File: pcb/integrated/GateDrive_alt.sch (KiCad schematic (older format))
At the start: 14 parts, among them U11001 UCC5350SB, U11002 R15P21503D

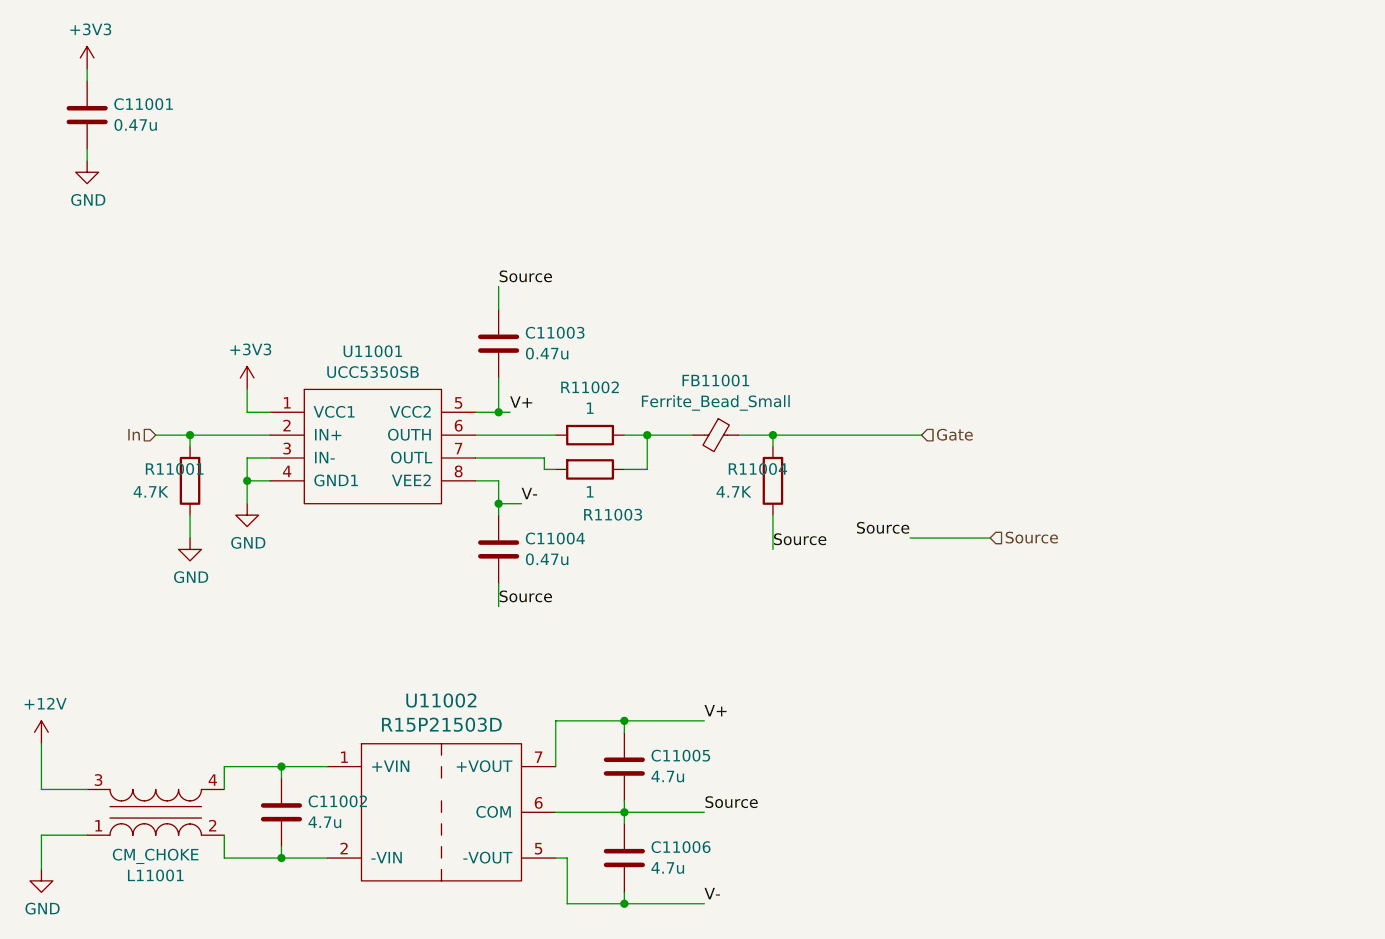
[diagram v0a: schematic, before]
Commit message: revised power input schematic
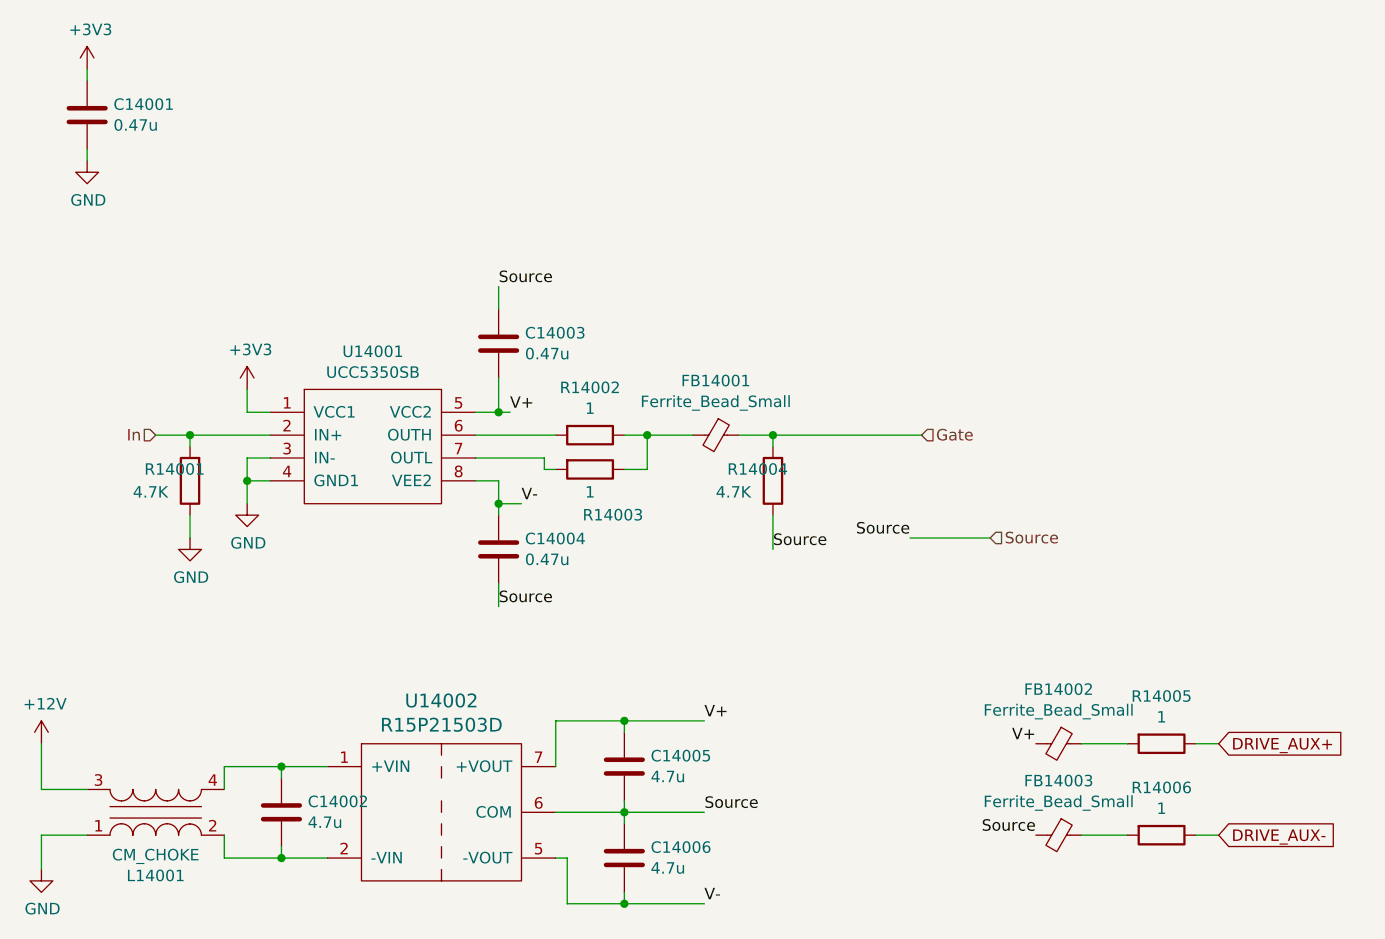
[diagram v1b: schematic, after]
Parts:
- added FB11002, FB11003: Ferrite_Bead_Small, Inductor_SMD:L_0805_2012Metric, symbol Device:Ferrite_Bead_Small
- added R11005, R11006: 1, Resistor_SMD:R_0805_2012Metric, symbol Device:R
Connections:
- net Source: now also FB11003.2
- net V+: now also FB11002.2
- new net: FB11002.1, R11005.2
- new net: FB11003.1, R11006.2
- new net DRIVE_AUX+: R11005.1
- new net DRIVE_AUX-: R11006.1
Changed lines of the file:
@@
 AR Path="/5D68A538/5D640674/5D6308ED" Ref="U13002"  Part="1"
 AR Path="/5D68A538/5D640682/5D6308ED" Ref="U14002"  Part="1"
-F 0 "U11002" H 3450 5237 60  0000 C CNN
+F 0 "U14002" H 3450 5237 60  0000 C CNN
 F 1 "R15P21503D" H 3450 5131 60  0000 C CNN
 F 2 "wbraun_smd:SIP7-5" H 3450 4850 60  0001 C CNN
@@
 AR Path="/5D68A538/5D640674/5D6308F4" Ref="U13001"  Part="1"
 AR Path="/5D68A538/5D640682/5D6308F4" Ref="U14001"  Part="1"
-F 0 "U11001" H 3150 3565 50  0000 C CNN
+F 0 "U14001" H 3150 3565 50  0000 C CNN
 F 1 "UCC5350SB" H 3150 3474 50  0000 C CNN
 F 2 "Package_SO:SOIC-8_3.9x4.9mm_P1.27mm" H 2800 3200 50  0001 C CNN
@@
 AR Path="/5D68A538/5D640674/5D6308FB" Ref="C13002"  Part="1"
 AR Path="/5D68A538/5D640682/5D6308FB" Ref="C14002"  Part="1"
-F 0 "C11002" H 2865 4796 50  0000 L CNN
+F 0 "C14002" H 2865 4796 50  0000 L CNN
 F 1 "4.7u" H 2865 4705 50  0000 L CNN
 F 2 "Capacitor_SMD:C_0805_2012Metric" H 2788 4600 50  0001 C CNN
@@
 AR Path="/5D68A538/5D640674/5D630902" Ref="C13005"  Part="1"
 AR Path="/5D68A538/5D640682/5D630902" Ref="C14005"  Part="1"
-F 0 "C11005" H 4365 4596 50  0000 L CNN
+F 0 "C14005" H 4365 4596 50  0000 L CNN
 F 1 "4.7u" H 4365 4505 50  0000 L CNN
 F 2 "Capacitor_SMD:C_0805_2012Metric" H 4288 4400 50  0001 C CNN
@@
 AR Path="/5D68A538/5D640674/5D630909" Ref="C13006"  Part="1"
 AR Path="/5D68A538/5D640682/5D630909" Ref="C14006"  Part="1"
-F 0 "C11006" H 4365 4996 50  0000 L CNN
+F 0 "C14006" H 4365 4996 50  0000 L CNN
 F 1 "4.7u" H 4365 4905 50  0000 L CNN
 F 2 "Capacitor_SMD:C_0805_2012Metric" H 4288 4800 50  0001 C CNN
@@
 AR Path="/5D68A538/5D640674/5D630910" Ref="C13003"  Part="1"
 AR Path="/5D68A538/5D640682/5D630910" Ref="C14003"  Part="1"
-F 0 "C11003" H 3815 2746 50  0000 L CNN
+F 0 "C14003" H 3815 2746 50  0000 L CNN
 F 1 "0.47u" H 3815 2655 50  0000 L CNN
 F 2 "Capacitor_SMD:C_0603_1608Metric" H 3738 2550 50  0001 C CNN
@@
 AR Path="/5D68A538/5D640674/5D630917" Ref="C13004"  Part="1"
 AR Path="/5D68A538/5D640682/5D630917" Ref="C14004"  Part="1"
-F 0 "C11004" H 3815 3646 50  0000 L CNN
+F 0 "C14004" H 3815 3646 50  0000 L CNN
 F 1 "0.47u" H 3815 3555 50  0000 L CNN
 F 2 "Capacitor_SMD:C_0603_1608Metric" H 3738 3450 50  0001 C CNN
@@
 AR Path="/5D68A538/5D640674/5D63091E" Ref="R13002"  Part="1"
 AR Path="/5D68A538/5D640682/5D63091E" Ref="R14002"  Part="1"
-F 0 "R11002" V 3893 3100 50  0000 C CNN
+F 0 "R14002" V 3893 3100 50  0000 C CNN
 F 1 "1" V 3984 3100 50  0000 C CNN
 F 2 "Resistor_SMD:R_0805_2012Metric" V 4030 3100 50  0001 C CNN
@@
 AR Path="/5D68A538/5D640674/5D630925" Ref="R13003"  Part="1"
 AR Path="/5D68A538/5D640682/5D630925" Ref="R14003"  Part="1"
-F 0 "R11003" V 4300 3350 50  0000 C CNN
+F 0 "R14003" V 4300 3350 50  0000 C CNN
 F 1 "1" V 4200 3250 50  0000 C CNN
 F 2 "Resistor_SMD:R_0805_2012Metric" V 4030 3250 50  0001 C CNN
@@
 AR Path="/5D68A538/5D640674/5D63093F" Ref="#PWR013007"  Part="1"
 AR Path="/5D68A538/5D640682/5D63093F" Ref="#PWR014007"  Part="1"
-F 0 "#PWR011007" H 2600 3150 50  0001 C CNN
+F 0 "#PWR014007" H 2600 3150 50  0001 C CNN
 F 1 "GND" H 2605 3227 50  0000 C CNN
 F 2 "" H 2600 3400 50  0001 C CNN
@@
 AR Path="/5D68A538/5D640674/5D630945" Ref="#PWR013006"  Part="1"
 AR Path="/5D68A538/5D640682/5D630945" Ref="#PWR014006"  Part="1"
-F 0 "#PWR011006" H 2600 2750 50  0001 C CNN
+F 0 "#PWR014006" H 2600 2750 50  0001 C CNN
 F 1 "+3V3" H 2615 3073 50  0000 C CNN
 F 2 "" H 2600 2900 50  0001 C CNN
@@
 AR Path="/5D68A538/5D640674/5D63094B" Ref="R13001"  Part="1"
 AR Path="/5D68A538/5D640682/5D63094B" Ref="R14001"  Part="1"
-F 0 "R11001" H 2550 3250 50  0000 R CNN
+F 0 "R14001" H 2550 3250 50  0000 R CNN
 F 1 "4.7K" H 2600 3350 50  0000 R CNN
 F 2 "Resistor_SMD:R_0603_1608Metric" V 2280 3300 50  0001 C CNN
@@
 AR Path="/5D68A538/5D640674/5D630955" Ref="#PWR013005"  Part="1"
 AR Path="/5D68A538/5D640682/5D630955" Ref="#PWR014005"  Part="1"
-F 0 "#PWR011005" H 2350 3300 50  0001 C CNN
+F 0 "#PWR014005" H 2350 3300 50  0001 C CNN
 F 1 "GND" H 2355 3377 50  0000 C CNN
 F 2 "" H 2350 3550 50  0001 C CNN
@@
 AR Path="/5D68A538/5D640674/5D630960" Ref="C13001"  Part="1"
 AR Path="/5D68A538/5D640682/5D630960" Ref="C14001"  Part="1"
-F 0 "C11001" H 2015 1746 50  0000 L CNN
+F 0 "C14001" H 2015 1746 50  0000 L CNN
 F 1 "0.47u" H 2015 1655 50  0000 L CNN
 F 2 "Capacitor_SMD:C_0603_1608Metric" H 1938 1550 50  0001 C CNN
@@
 AR Path="/5D68A538/5D640674/5D630967" Ref="#PWR013003"  Part="1"
 AR Path="/5D68A538/5D640682/5D630967" Ref="#PWR014003"  Part="1"
-F 0 "#PWR011003" H 1900 1350 50  0001 C CNN
+F 0 "#PWR014003" H 1900 1350 50  0001 C CNN
 F 1 "+3V3" H 1915 1673 50  0000 C CNN
 F 2 "" H 1900 1500 50  0001 C CNN
@@
 AR Path="/5D68A538/5D640674/5D63096D" Ref="#PWR013004"  Part="1"
 AR Path="/5D68A538/5D640682/5D63096D" Ref="#PWR014004"  Part="1"
-F 0 "#PWR011004" H 1900 1650 50  0001 C CNN
+F 0 "#PWR014004" H 1900 1650 50  0001 C CNN
 F 1 "GND" H 1905 1727 50  0000 C CNN
 F 2 "" H 1900 1900 50  0001 C CNN
@@
 AR Path="/5D68A538/5D640674/5D634CBC" Ref="#PWR013002"  Part="1"
 AR Path="/5D68A538/5D640682/5D634CBC" Ref="#PWR014002"  Part="1"
-F 0 "#PWR011002" H 1700 4750 50  0001 C CNN
+F 0 "#PWR014002" H 1700 4750 50  0001 C CNN
 F 1 "GND" H 1705 4827 50  0000 C CNN
 F 2 "" H 1700 5000 50  0001 C CNN
@@
 AR Path="/5D68A538/5D640674/5D634D09" Ref="#PWR013001"  Part="1"
 AR Path="/5D68A538/5D640682/5D634D09" Ref="#PWR014001"  Part="1"
-F 0 "#PWR011001" H 1700 4300 50  0001 C CNN
+F 0 "#PWR014001" H 1700 4300 50  0001 C CNN
 F 1 "+12V" H 1715 4623 50  0000 C CNN
 F 2 "" H 1700 4450 50  0001 C CNN
@@
 AR Path="/5D68A538/5D640674/5D63A672" Ref="FB13001"  Part="1"
 AR Path="/5D68A538/5D640682/5D63A672" Ref="FB14001"  Part="1"
-F 0 "FB11001" V 4413 3100 50  0000 C CNN
+F 0 "FB14001" V 4413 3100 50  0000 C CNN
 F 1 "Ferrite_Bead_Small" V 4504 3100 50  0000 C CNN
 F 2 "Inductor_SMD:L_0805_2012Metric" V 4580 3100 50  0001 C CNN
@@
 AR Path="/5D68A538/5D640674/5D63A754" Ref="R13004"  Part="1"
 AR Path="/5D68A538/5D640682/5D63A754" Ref="R14004"  Part="1"
-F 0 "R11004" H 5100 3250 50  0000 R CNN
+F 0 "R14004" H 5100 3250 50  0000 R CNN
 F 1 "4.7K" H 5150 3350 50  0000 R CNN
 F 2 "Resistor_SMD:R_0603_1608Metric" V 4830 3300 50  0001 C CNN
@@
 AR Path="/5D68A538/5D640674/5D63092C" Ref="L13001"  Part="1"
 AR Path="/5D68A538/5D640682/5D63092C" Ref="L14001"  Part="1"
-F 0 "L11001" H 2200 5028 50  0000 C CNN
+F 0 "L14001" H 2200 5028 50  0000 C CNN
 F 1 "CM_CHOKE" H 2200 4937 50  0000 C CNN
 F 2 "wbraun_smd:SRF2012" V 2200 4750 50  0001 C CNN
@@
 	1    0    0    1
 $EndComp
+$Comp
+L Device:R R?
+U 1 1 5DCA72F3
+P 6600 4450
+AR Path="/5D68A538/5DCA72F3" Ref="R?"  Part="1"
+AR Path="/5D68A538/5D62FC9C/5DCA72F3" Ref="R11005"  Part="1"
+AR Path="/5D68A538/5D640666/5DCA72F3" Ref="R12005"  Part="1"
+AR Path="/5D68A538/5D640674/5DCA72F3" Ref="R13005"  Part="1"
+AR Path="/5D68A538/5D640682/5DCA72F3" Ref="R14005"  Part="1"
+F 0 "R14005" V 6393 4450 50  0000 C CNN
+F 1 "1" V 6484 4450 50  0000 C CNN
+F 2 "Resistor_SMD:R_0805_2012Metric" V 6530 4450 50  0001 C CNN
+F 3 "~" H 6600 4450 50  0001 C CNN
+	1    6600 4450
+	0    1    1    0
+$EndComp
+$Comp
+L Device:R R?
+U 1 1 5DCA9067
+P 6600 4850
+AR Path="/5D68A538/5DCA9067" Ref="R?"  Part="1"
+AR Path="/5D68A538/5D62FC9C/5DCA9067" Ref="R11006"  Part="1"
+AR Path="/5D68A538/5D640666/5DCA9067" Ref="R12006"  Part="1"
+AR Path="/5D68A538/5D640674/5DCA9067" Ref="R13006"  Part="1"
+AR Path="/5D68A538/5D640682/5DCA9067" Ref="R14006"  Part="1"
+F 0 "R14006" V 6393 4850 50  0000 C CNN
+F 1 "1" V 6484 4850 50  0000 C CNN
+F 2 "Resistor_SMD:R_0805_2012Metric" V 6530 4850 50  0001 C CNN
+F 3 "~" H 6600 4850 50  0001 C CNN
+	1    6600 4850
+	0    1    1    0
+$EndComp
+Wire Wire Line
+	6750 4450 6850 4450
+Wire Wire Line
+	6750 4850 6850 4850
+Text GLabel 6850 4450 2    50   Input ~ 0
+DRIVE_AUX+
+Text GLabel 6850 4850 2    50   Input ~ 0
+DRIVE_AUX-
+$Comp
+L Device:Ferrite_Bead_Small FB11002
+U 1 1 5DCADBEB
+P 6150 4450
+AR Path="/5D68A538/5D62FC9C/5DCADBEB" Ref="FB11002"  Part="1"
+AR Path="/5D68A538/5D640666/5DCADBEB" Ref="FB12002"  Part="1"
+AR Path="/5D68A538/5D640674/5DCADBEB" Ref="FB13002"  Part="1"
+AR Path="/5D68A538/5D640682/5DCADBEB" Ref="FB14002"  Part="1"
+F 0 "FB14002" V 5913 4450 50  0000 C CNN
+F 1 "Ferrite_Bead_Small" V 6004 4450 50  0000 C CNN
+F 2 "Inductor_SMD:L_0805_2012Metric" V 6080 4450 50  0001 C CNN
+F 3 "~" H 6150 4450 50  0001 C CNN
+	1    6150 4450
+	0    1    1    0
+$EndComp
+$Comp
+L Device:Ferrite_Bead_Small FB11003
+U 1 1 5DCAE3FD
+P 6150 4850
+AR Path="/5D68A538/5D62FC9C/5DCAE3FD" Ref="FB11003"  Part="1"
+AR Path="/5D68A538/5D640666/5DCAE3FD" Ref="FB12003"  Part="1"
+AR Path="/5D68A538/5D640674/5DCAE3FD" Ref="FB13003"  Part="1"
+AR Path="/5D68A538/5D640682/5DCAE3FD" Ref="FB14003"  Part="1"
+F 0 "FB14003" V 5913 4850 50  0000 C CNN
+F 1 "Ferrite_Bead_Small" V 6004 4850 50  0000 C CNN
+F 2 "Inductor_SMD:L_0805_2012Metric" V 6080 4850 50  0001 C CNN
+F 3 "~" H 6150 4850 50  0001 C CNN
+	1    6150 4850
+	0    1    1    0
+$EndComp
+Wire Wire Line
+	6250 4450 6450 4450
+Wire Wire Line
+	6250 4850 6450 4850
+Text Label 6050 4450 2    50   ~ 0
+V+
+Text Label 6050 4850 2    50   ~ 0
+Source
 $EndSCHEMATC

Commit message: routing, all componens placed on PCB
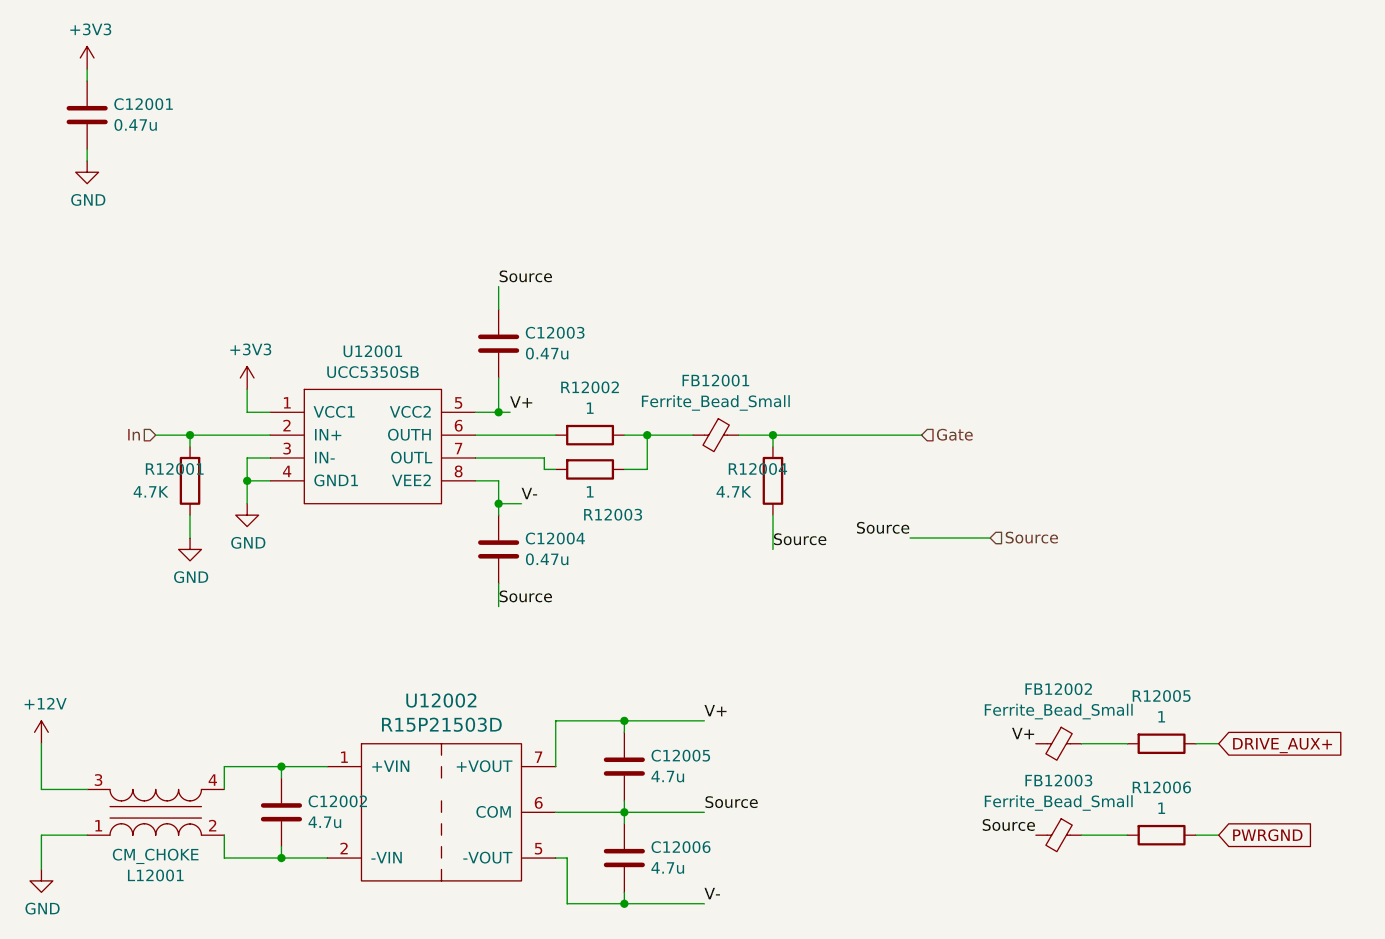
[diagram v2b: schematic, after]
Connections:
- net DRIVE_AUX- renamed PWRGND

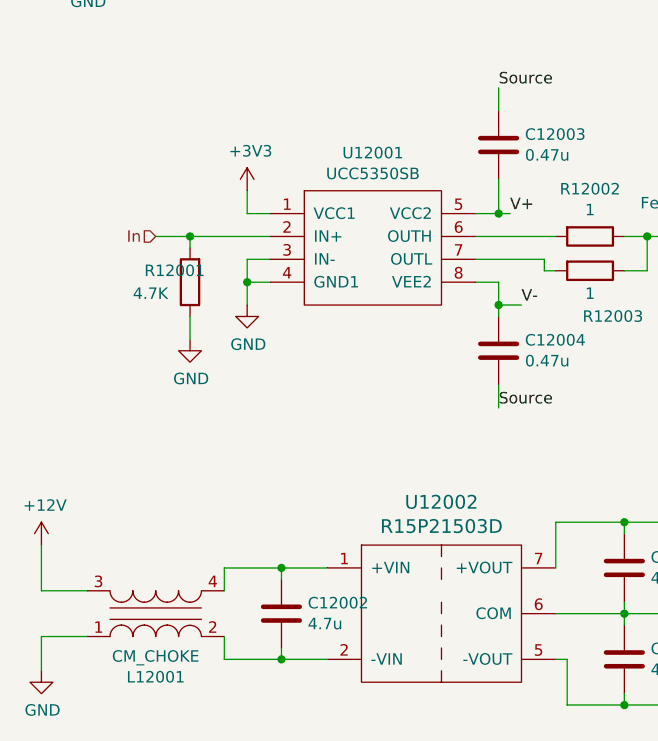
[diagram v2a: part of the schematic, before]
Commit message: updated component values for schematic
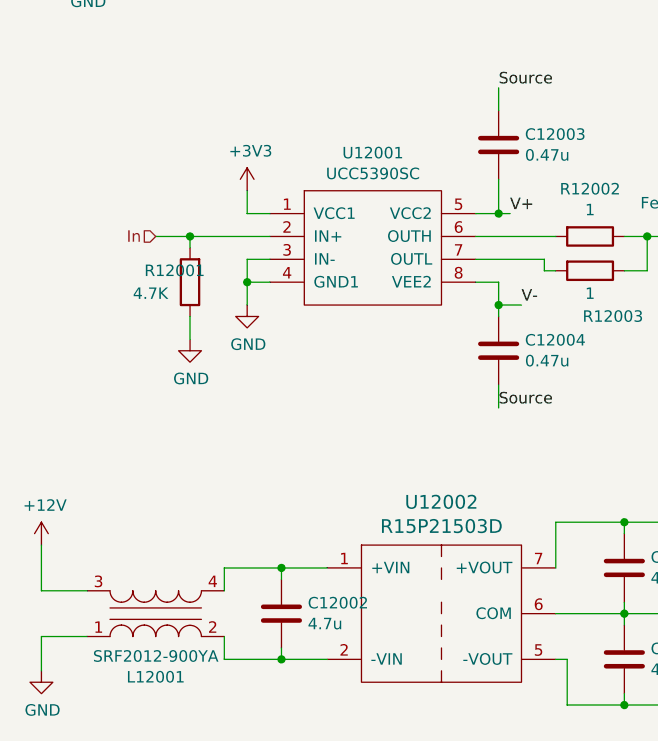
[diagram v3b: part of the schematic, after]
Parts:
- L11001: value CM_CHOKE -> SRF2012-900YA
- U11001: value UCC5350SB -> UCC5390SC
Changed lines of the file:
@@
 EESchema Schematic File Version 4
 LIBS:integrated-cache
-EELAYER 30 0
+EELAYER 26 0
 EELAYER END
 $Descr A4 11693 8268
@@
 AR Path="/5D68A538/5D640682/5D6308F4" Ref="U14001"  Part="1"
 F 0 "U12001" H 3150 3565 50  0000 C CNN
-F 1 "UCC5350SB" H 3150 3474 50  0000 C CNN
+F 1 "UCC5390SC" H 3150 3474 50  0000 C CNN
 F 2 "Package_SO:SOIC-8_3.9x4.9mm_P1.27mm" H 2800 3200 50  0001 C CNN
 F 3 "" H 2800 3200 50  0001 C CNN
@@
 AR Path="/5D68A538/5D640682/5DD374BE" Ref="L14001"  Part="1"
 F 0 "L12001" H 2200 5028 50  0000 C CNN
-F 1 "CM_CHOKE" H 2200 4937 50  0000 C CNN
+F 1 "SRF2012-900YA" H 2200 4937 50  0000 C CNN
 F 2 "wbraun_smd:SRF2012" V 2200 4750 50  0001 C CNN
 F 3 "" V 2200 4750 50  0000 C CNN
